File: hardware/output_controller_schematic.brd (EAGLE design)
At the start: 100 x 75 mm, 49 parts, among them IC1 PIC16F1939-I_P, IC2 DAC102S085CIMM_NOPB, IC3 LM6211MF, IC4 LM6211MF, IC5 MIC4575-5.0WU_TR, Q1 IRF1010NSPBF, Q2 IRF1010NSPBF, Q3 IRF1010NSPBF, Q4 IRF1010NSPBF, Y1 20MHz

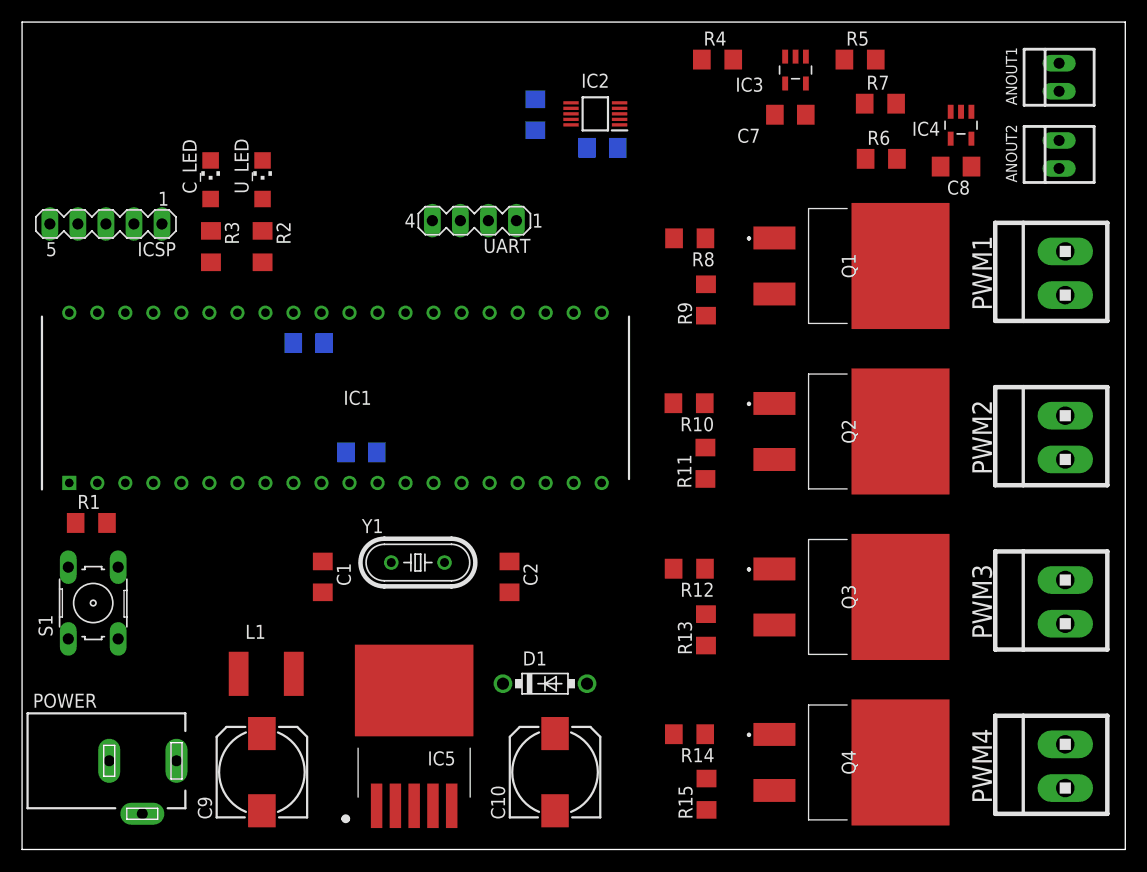
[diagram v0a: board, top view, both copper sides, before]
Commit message: start code and simulation with blinking leds
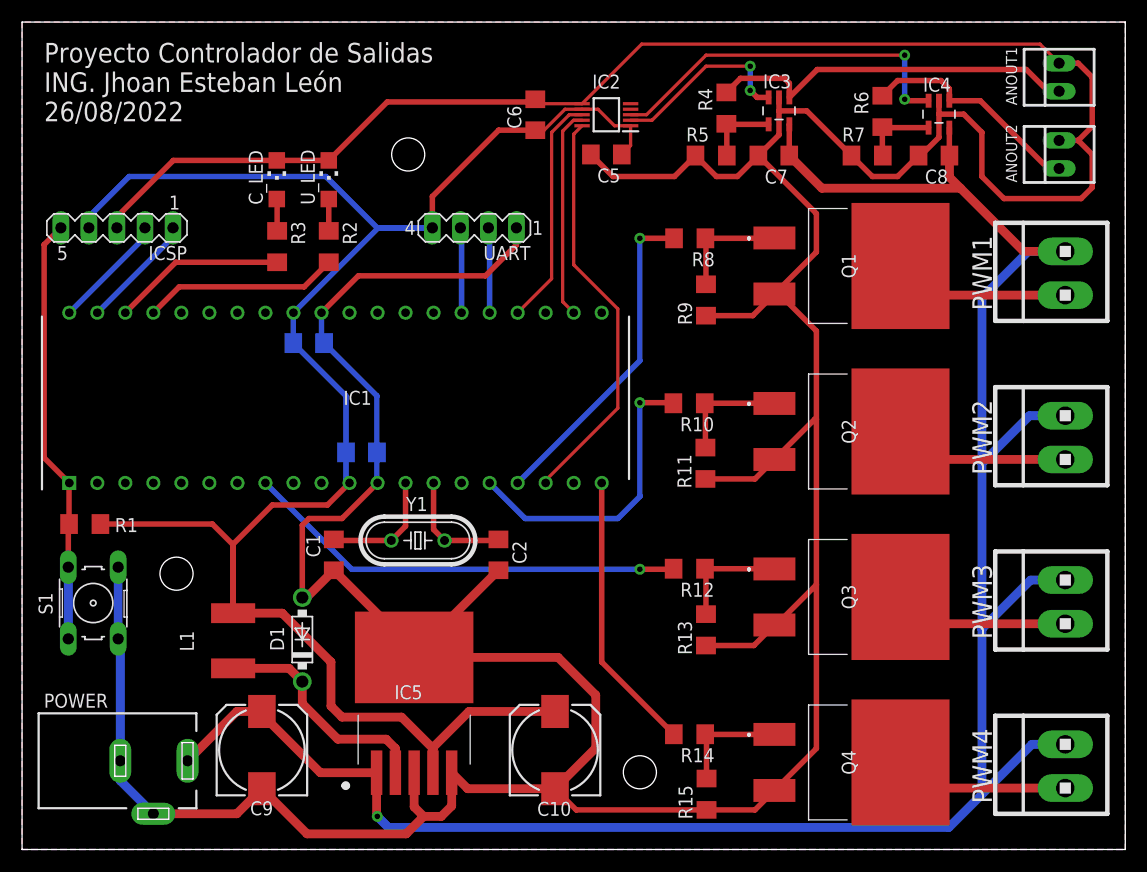
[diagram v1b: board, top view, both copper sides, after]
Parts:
- moved D1 22.4 mm to (25.4, 19.0), turned to 90 degrees
- moved R5 16.1 mm to (62.5, 62.9)
- moved C_LED 6.00 mm to (23.1, 60.7)
- moved R2 6.00 mm to (27.8, 54.6)
- moved R3 6.00 mm to (23.1, 54.6)
- moved U_LED 6.00 mm to (27.8, 60.7)
- moved R7 4.85 mm to (76.6, 62.9)
- moved R4 4.47 mm to (63.8, 67.2), turned to 90 degrees
- moved R6 4.30 mm to (78.0, 66.9), turned to 90 degrees
- moved L1 4.24 mm to (19.1, 18.9), turned to 270 degrees
- moved IC3 3.99 mm to (68.6, 67.0)
- moved C7 3.99 mm to (68.1, 62.9)
- moved IC5 3.00 mm to (34.9, 11.5)
- moved C1 2.24 mm to (28.3, 26.7)
- moved C2 2.24 mm to (43.2, 26.7)
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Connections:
- net CS: now also IC1.22; no longer IC1.15
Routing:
- net GND: track 0.00 -> 477.0 mm
- net +24V: track 0.00 -> 201.7 mm, vias 0 -> 1
- net +5V: track 0.00 -> 177.1 mm
- net PWM3: track 0.00 -> 40.3 mm, vias 0 -> 1
- net RESET: track 0.00 -> 38.9 mm
- net SCK: track 0.00 -> 37.1 mm
- net AN1: track 0.00 -> 34.0 mm
- net VOUT2: track 0.00 -> 33.3 mm, vias 0 -> 2
- net PWM1: track 0.00 -> 29.9 mm, vias 0 -> 1
- net PWM2: track 0.00 -> 27.3 mm, vias 0 -> 1
- net PWM4: track 0.00 -> 25.5 mm
- net N$18: track 0.00 -> 21.1 mm
- net SDO: track 0.00 -> 21.0 mm
- net AN2: track 0.00 -> 20.5 mm
- net CS: track 0.00 -> 19.0 mm
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- added copper zone on layer 1, net GND
- added copper zone on layer 16, net GND
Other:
- board text added: "Proyecto Controlador de Salidas ING. Jhoan Esteban León 26/08/2022"
